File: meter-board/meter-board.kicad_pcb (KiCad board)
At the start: 4 copper layers, 100 x 50 mm, 291 parts, among them J1 2-1445053-2, J2 3-794636-8, J3 2-1445053-4, Q1 PMN100EPAX, Q2 2N7002K-AU_R1_000A2, U1 AP66300QFVBW-13, U10 TLV1814RTER, U11 TLV1814RTER, U12 TLV1814RTER, U13 TLV1814RTER, U14 TLV1814RTER, U15 TLV1814RTER, U16 TBD62183AFNG,EL, U17 TBD62183AFNG,EL, U18 TBD62183AFNG,EL, U19 TBD62183AFNG,EL, U2 TS431BIYLT, U20 TLV1814RTER, U21 SN74HC595BRWNR, U22 SN74HC595BRWNR, U23 SN74HC595BRWNR, U24 TBD62783AFNG,EL, U25 TBD62183AFNG,EL, U26 TBD62183AFNG,EL, U27 SN74LV4T125RGYR, U3 ACSC02-41SURKWA-F01, U4 ACSC02-41SURKWA-F01, U5 ACSC02-41SURKWA-F01, U6 157121S12700, U7 157121S12700, U8 157121S12700, U9 TLV1814RTER

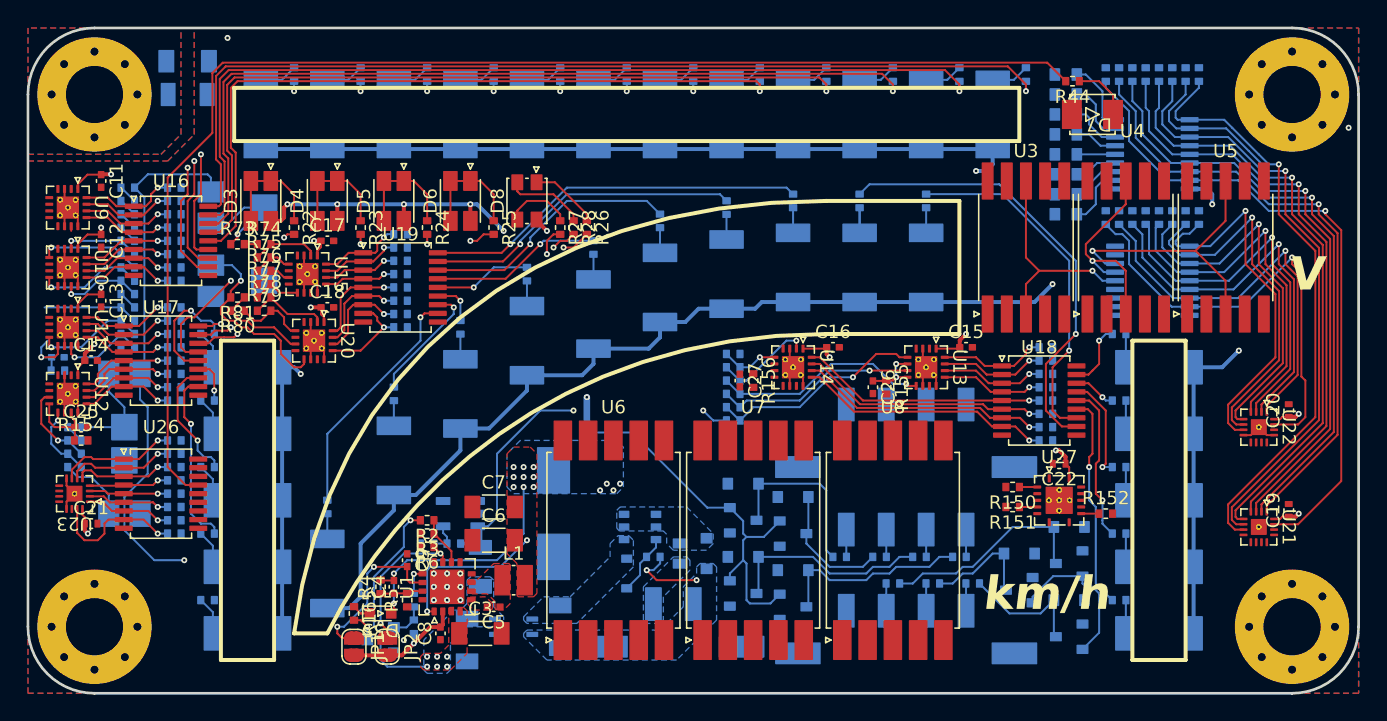
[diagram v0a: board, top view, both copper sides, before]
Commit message: update patterns
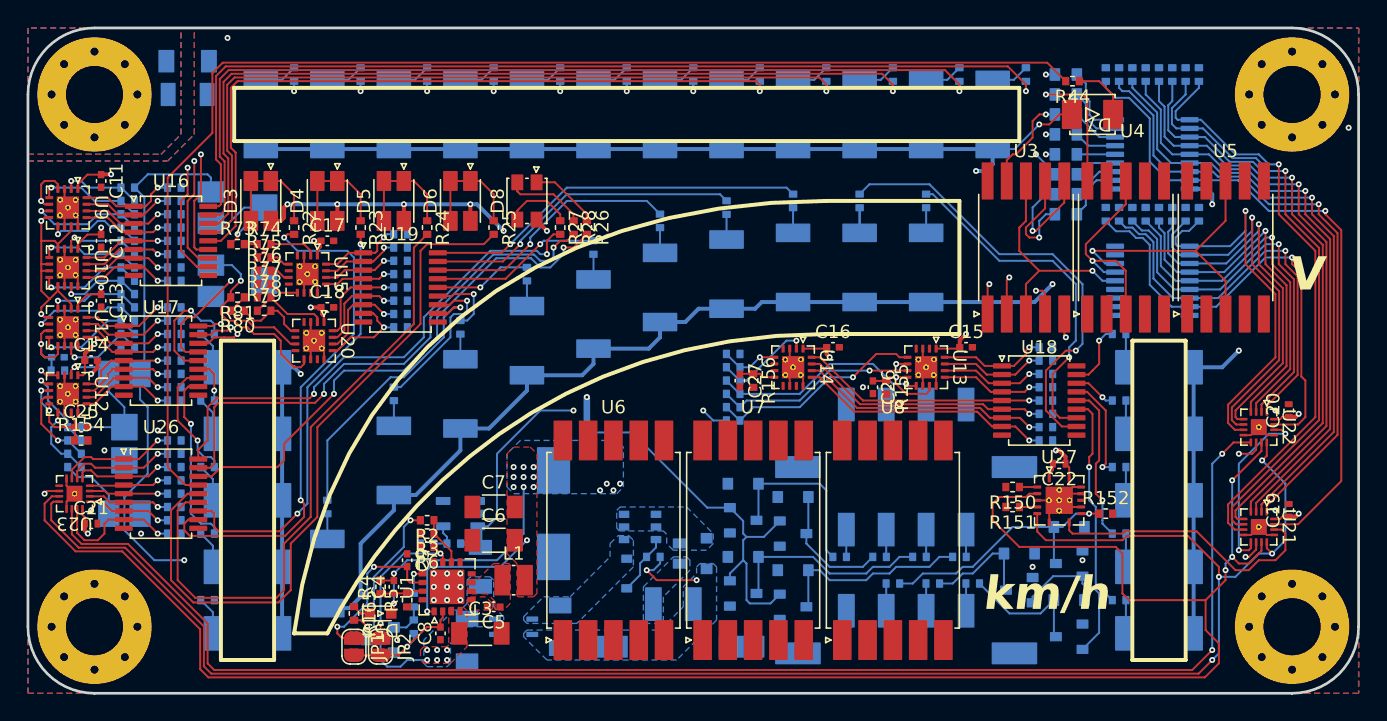
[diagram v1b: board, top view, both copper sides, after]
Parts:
- moved JP2 0.50 mm to (26.5, 46.5)
- moved R134 0.25 mm to (88.0, 14.0)
- moved R135 0.25 mm to (87.0, 14.0)
- moved R136 0.25 mm to (86.0, 14.0)
- moved R137 0.25 mm to (85.0, 14.0)
- moved R138 0.25 mm to (84.0, 14.0)
- moved R139 0.25 mm to (83.0, 14.0)
- moved R140 0.25 mm to (82.0, 14.0)
- moved R141 0.25 mm to (81.0, 14.0)
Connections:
- net /W5_W1 renamed /W4_W1
- net /W5_W2 renamed /W4_W2
- R24 pad 2: /W5_W4 -> /W4_W3
- R25 pad 2: /W5_W3 -> /W4_W4
- U26 pad 13: /W5_W3 -> /W4_W3
- U26 pad 14: /W5_W4 -> /W4_W4
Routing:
- net Net-(U21-SRCLK): track 0.00 -> 145.3 mm, vias 0 -> 3
- net Net-(U21-RCLK): track 0.00 -> 135.1 mm, vias 0 -> 4
- net Net-(U22-QH'): track 0.00 -> 111.8 mm, vias 0 -> 2
- net /W4_W4: track 0.00 -> 53.4 mm
- net /W4_W3: track 0.00 -> 47.0 mm
- net /W4_W1: track 0.85 -> 39.4 mm, vias 1 -> 2
- net /RGB_G: track 1.91 -> 40.1 mm, vias 1 -> 2
- net /RGB_R: track 2.16 -> 39.8 mm, vias 1 -> 2
- net /RGB_B: track 2.20 -> 38.0 mm, vias 1 -> 2
- net /W4_W2: track 0.74 -> 32.7 mm, vias 1 -> 2
- net /G6R6_AIN: track 18.9 -> 45.2 mm, vias 1 -> 4
- net +5VD: track 308.0 -> 334.2 mm, vias 32 -> 36
- net /7seg_DP: track 0.00 -> 22.8 mm, vias 0 -> 2
- net Net-(U21-SER): track 0.00 -> 21.1 mm
- net /7seg_C: track 0.00 -> 20.2 mm, vias 0 -> 2
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
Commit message: update patterns
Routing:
- net /R5_R1: track 0.00 -> 98.8 mm, vias 0 -> 4
- net Net-(U13A--): track 5.37 -> 87.6 mm, vias 0 -> 1
- net Net-(U14D--): track 0.98 -> 60.1 mm, vias 0 -> 3
- net Net-(U14C--): track 8.28 -> 65.6 mm, vias 1 -> 3
- net /7seg_CC1: track 0.00 -> 53.6 mm, vias 0 -> 1
- net /7seg_CC2: track 0.00 -> 43.7 mm, vias 0 -> 1
- net /7seg_CC3: track 0.00 -> 31.8 mm, vias 0 -> 1
- net /R10_AIN: track 17.4 -> 27.7 mm, vias 0 -> 4
- net /G5_AIN: track 17.9 -> 22.7 mm
- net /W4_W1: track 39.4 -> 38.1 mm
- net Net-(U15D--): track 3.69 -> 4.55 mm
- net Net-(U13D--): track 16.3 -> 17.1 mm
- net /VIN: track 16.5 -> 17.3 mm
- net Net-(U15B--): track 2.98 -> 3.78 mm
- net GND: track 50.6 -> 50.8 mm, vias 24 -> 29

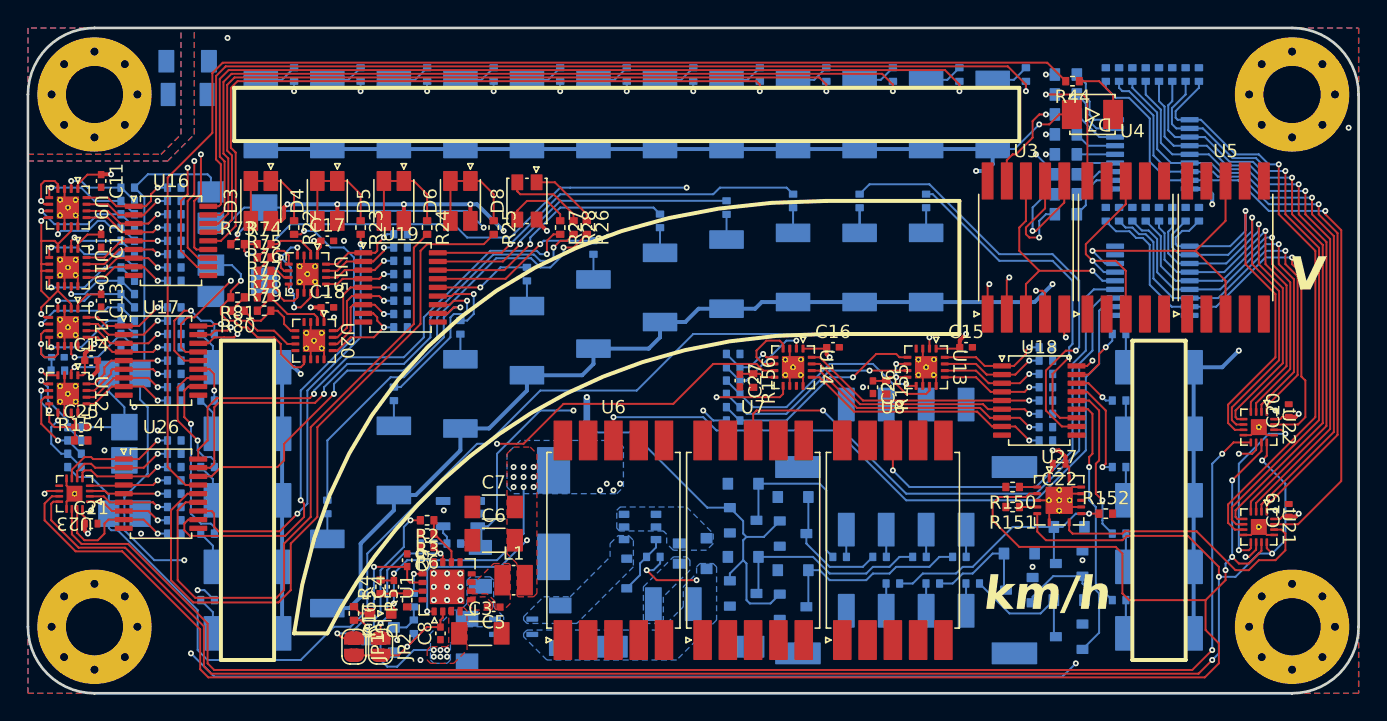
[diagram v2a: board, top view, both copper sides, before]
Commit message: update patterns
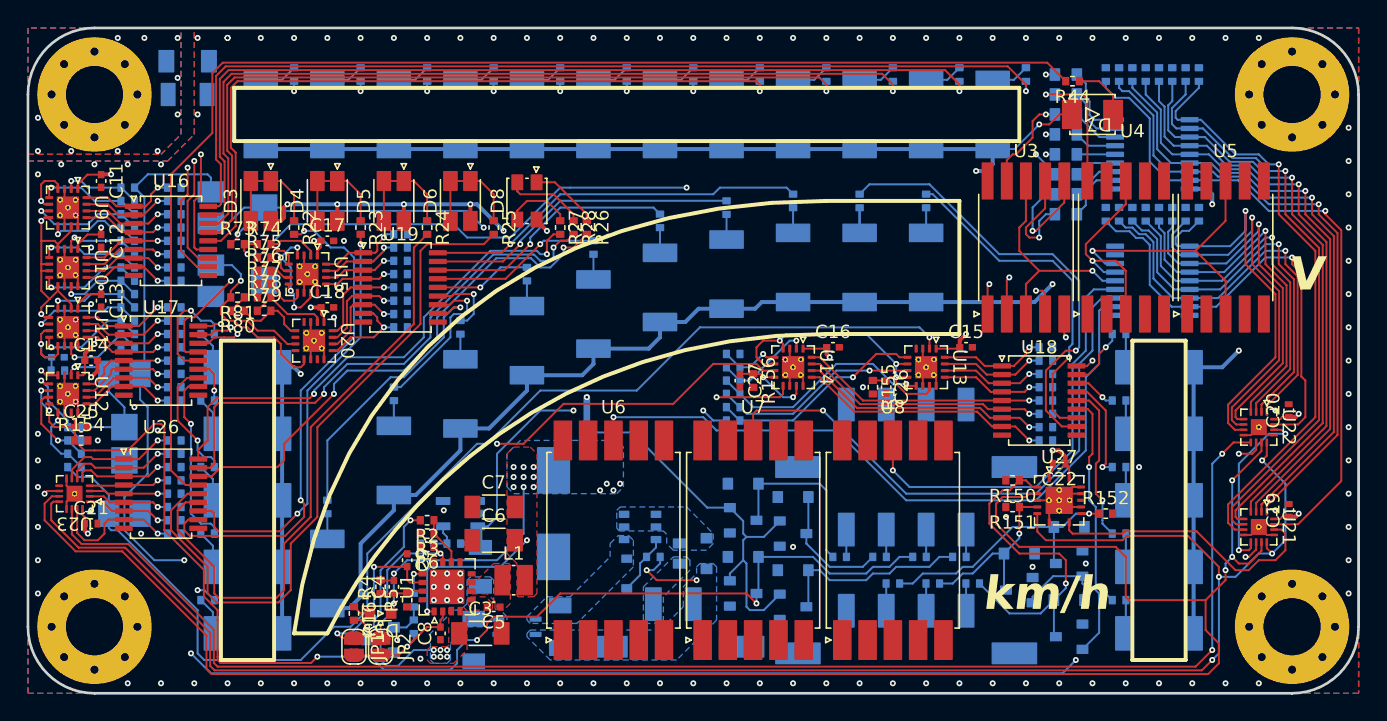
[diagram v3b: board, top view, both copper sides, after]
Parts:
- moved C26 1.00 mm to (64.5, 27.0)
- moved R155 1.00 mm to (63.5, 27.0)
- moved C2 0.50 mm to (33.5, 46.0)
- moved R150 0.50 mm to (74.0, 34.0)
- moved FL1 0.25 mm to (36.8, 45.0)
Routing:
- net /R5_AIN: track 26.8 -> 99.4 mm, vias 3 -> 6
- net /SR_CLK: track 11.1 -> 26.0 mm, vias 0 -> 1
- net /G5_AIN: track 22.7 -> 32.8 mm, vias 2 -> 3
- net /SR_~{CS}: track 9.92 -> 13.9 mm, vias 0 -> 1
- net /R10_AIN: track 27.7 -> 31.5 mm, vias 4 -> 6
- net +5VA: track 181.1 -> 182.2 mm
- net /W4_W3: track 47.0 -> 46.0 mm
- net /W4_W4: track 53.4 -> 52.4 mm
- net Net-(U21-SRCLK): track 145.3 -> 144.4 mm
- net Net-(U13A--): track 87.6 -> 88.1 mm
- net Net-(U22-QH'): track 111.8 -> 111.3 mm
- net Net-(U21-RCLK): track 135.1 -> 134.6 mm
- net GND: vias 29 -> 126
- net Chassis: vias 0 -> 10

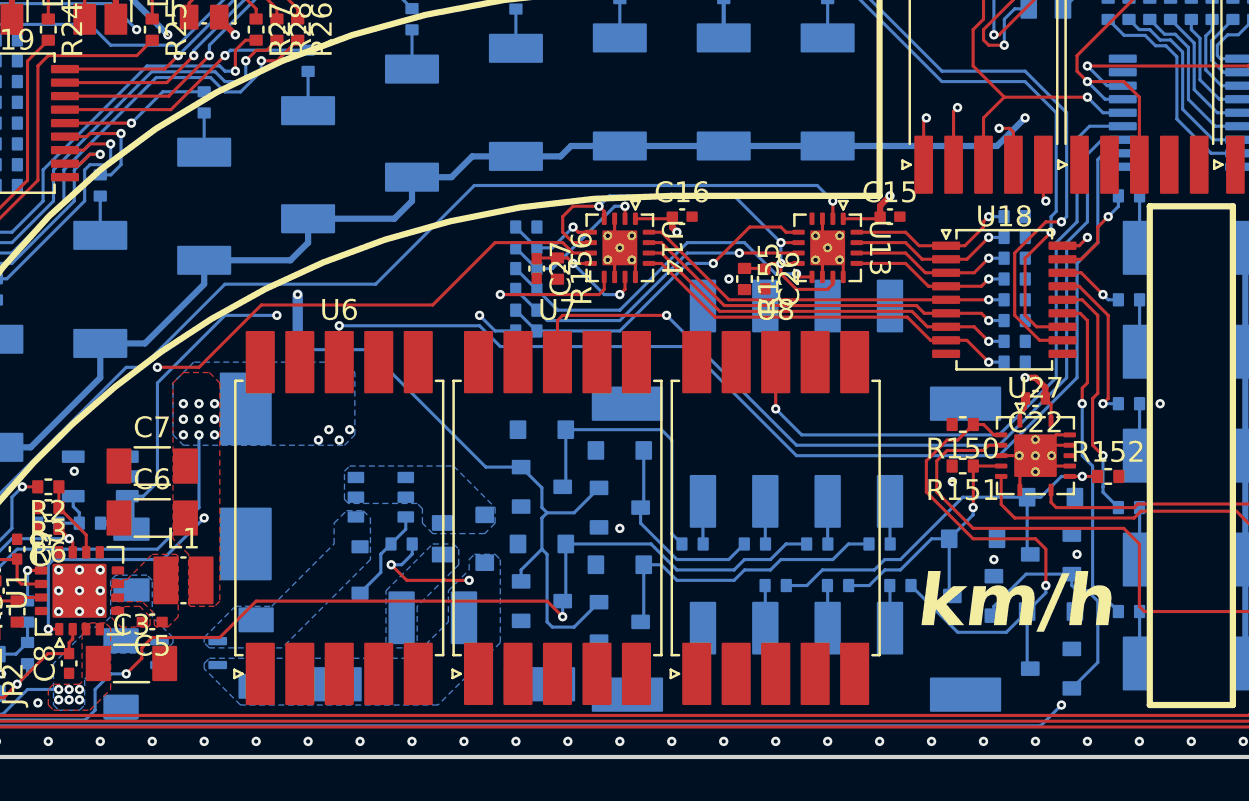
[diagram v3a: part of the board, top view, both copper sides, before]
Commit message: update patterns
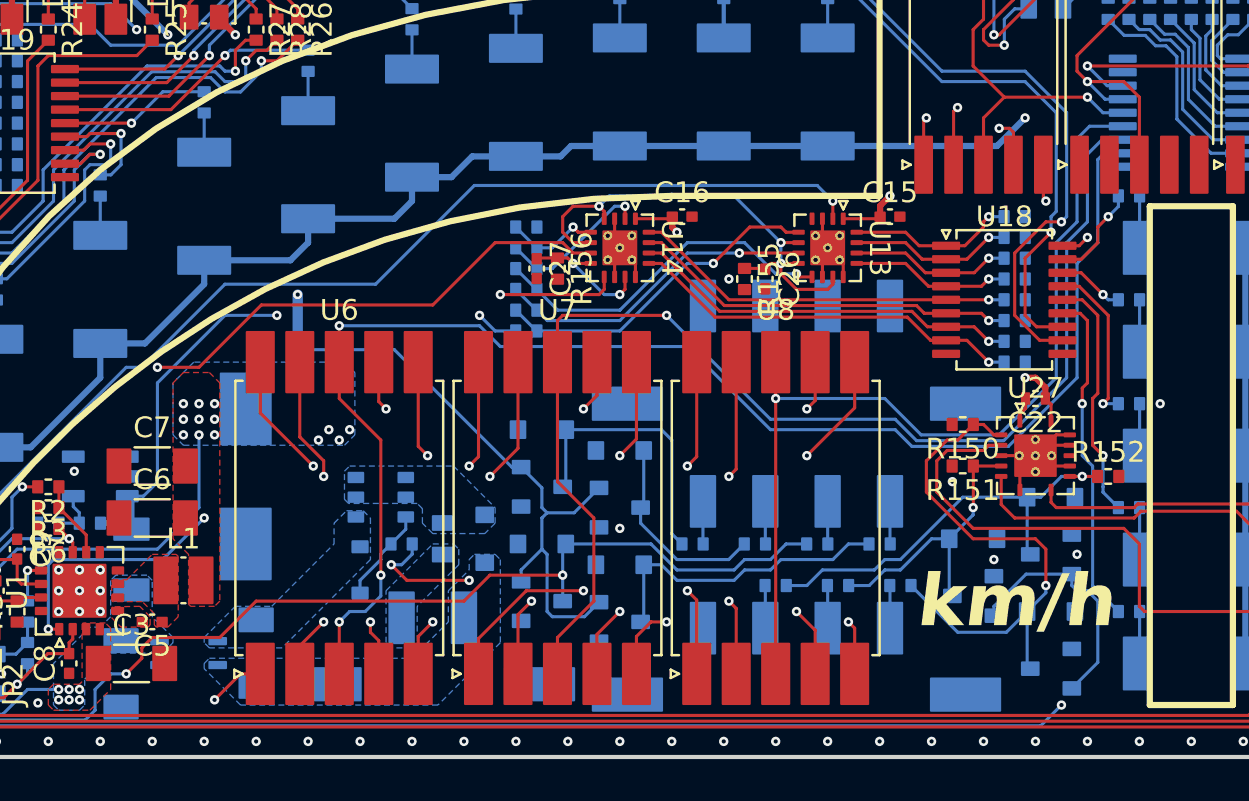
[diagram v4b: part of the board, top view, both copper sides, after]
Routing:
- net /7seg_E: track 17.4 -> 57.0 mm, vias 2 -> 5
- net /7seg_F: track 7.33 -> 44.5 mm, vias 1 -> 4
- net /7seg_G: track 10.1 -> 44.5 mm, vias 1 -> 4
- net /7seg_B: track 8.72 -> 41.9 mm, vias 1 -> 4
- net /7seg_D: track 13.9 -> 44.2 mm, vias 2 -> 5
- net /7seg_C: track 20.2 -> 50.4 mm, vias 2 -> 5
- net /7seg_DP: track 22.8 -> 51.8 mm, vias 2 -> 5
- net /7seg_A: track 8.33 -> 35.9 mm, vias 1 -> 4
- net /7seg_CC1: track 53.6 -> 70.4 mm, vias 1 -> 3
- net /7seg_CC2: track 43.7 -> 60.0 mm
- net /7seg_CC3: track 31.8 -> 44.7 mm
- net +5VREF: track 120.1 -> 119.0 mm
- net +5VD: track 334.2 -> 333.3 mm
- net +5VA: track 182.2 -> 181.5 mm
- net /R5_AIN: track 99.4 -> 98.9 mm
